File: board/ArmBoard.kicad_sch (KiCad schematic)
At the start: 0 parts

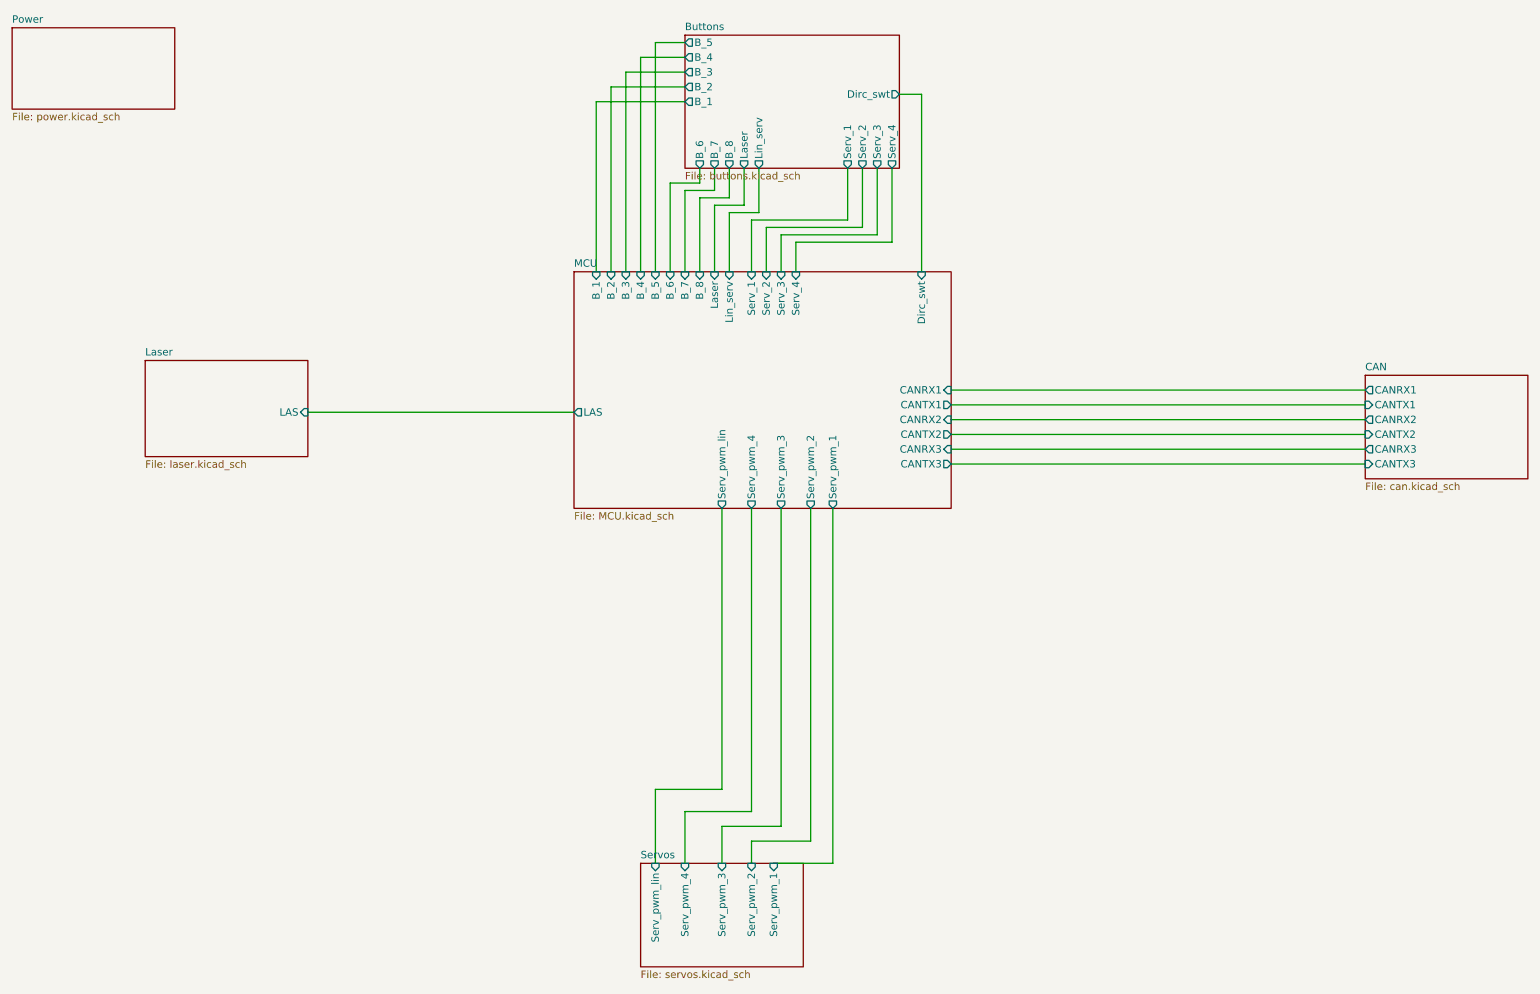
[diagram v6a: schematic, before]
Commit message: Schematic review changes part 2 the electric boogaloo
finished fixing schematic. Made better names for heiracal pins. Made LED ressistors standard values.
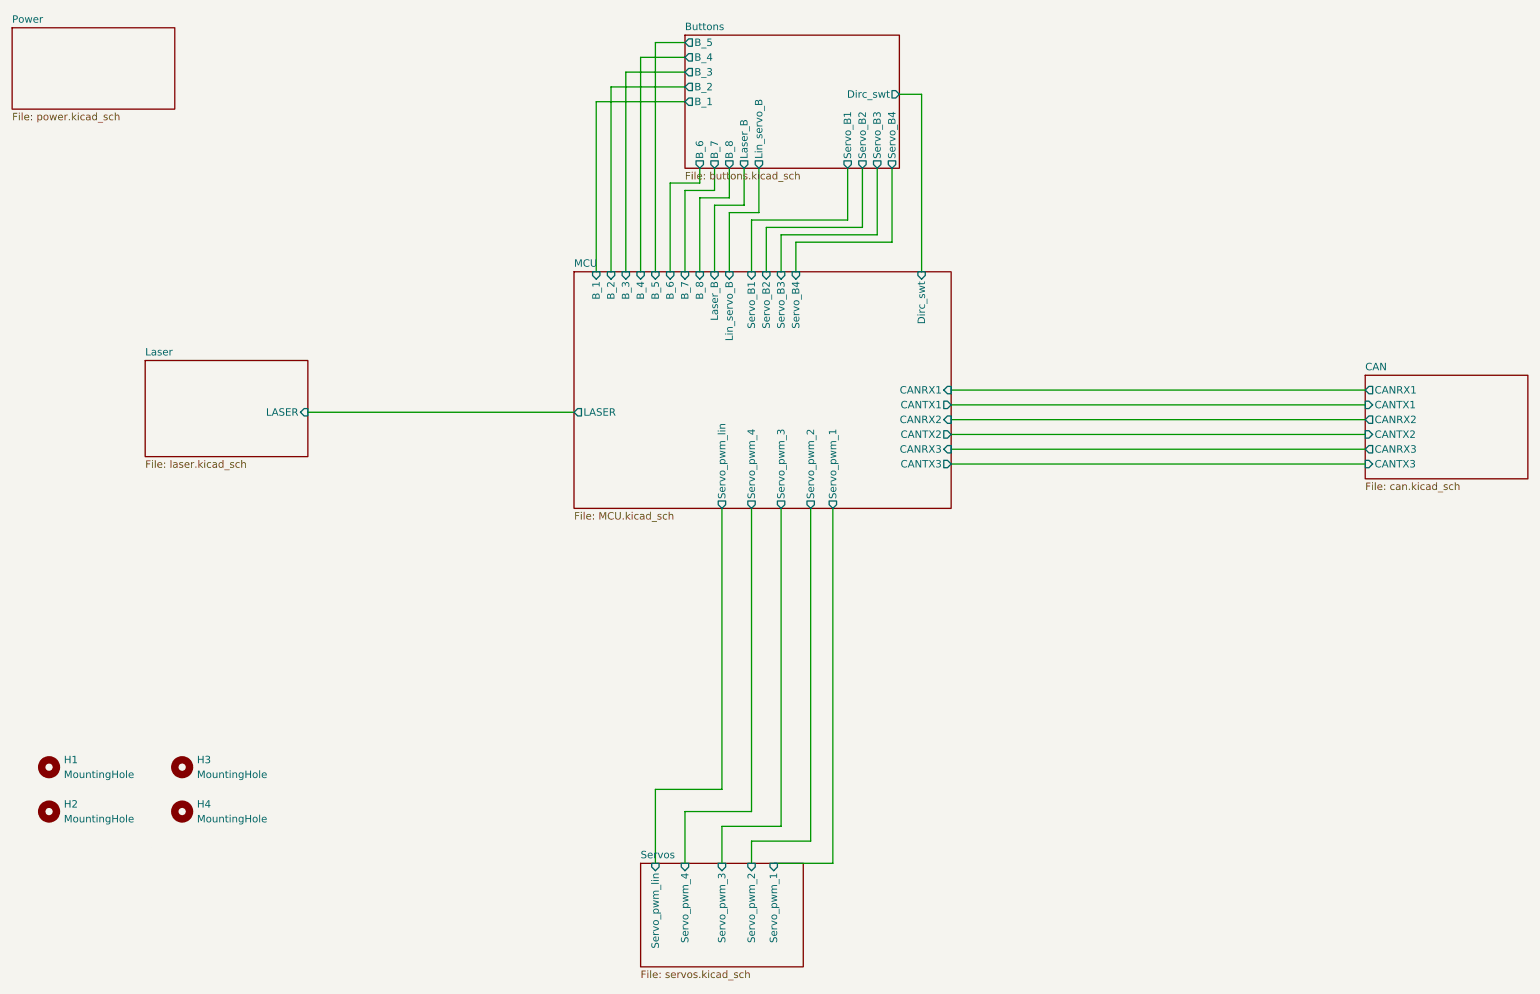
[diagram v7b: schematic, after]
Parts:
- added H1, H2, H3, H4: MountingHole, symbol Mechanical:MountingHole
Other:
- sheet Buttons ports: added Laser_B, Lin_servo_B, Servo_B1, Servo_B2, Servo_B3, Servo_B4; removed Laser, Lin_serv, Serv_1, Serv_2, Serv_3, Serv_4
- sheet Laser ports: added LASER; removed LAS
- sheet MCU ports: added LASER, Laser_B, Lin_servo_B, Servo_B1, Servo_B2, Servo_B3, Servo_B4, Servo_pwm_1, Servo_pwm_2, Servo_pwm_3, Servo_pwm_4, Servo_pwm_lin; removed LAS, Laser, Lin_serv, Serv_1, Serv_2, Serv_3, Serv_4, Serv_pwm_1, Serv_pwm_2, Serv_pwm_3, Serv_pwm_4, Serv_pwm_lin
- sheet Servos ports: added Servo_pwm_1, Servo_pwm_2, Servo_pwm_3, Servo_pwm_4, Servo_pwm_lin; removed Serv_pwm_1, Serv_pwm_2, Serv_pwm_3, Serv_pwm_4, Serv_pwm_lin
- note added: "Penis"

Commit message: Prototype Layout
Made an initial Layout to be edited and changed uwu
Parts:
- H1, H2, H3, H4: footprint (none) -> MRDT_Drill_Holes:4_40_Hole_Corner
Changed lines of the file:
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@@
 			)
 		)
-		(property "Footprint" ""
+		(property "Footprint" "MRDT_Drill_Holes:4_40_Hole_Corner"
 			(at 26.67 149.86 0)
 			(effects
@@
 			)
 		)
-		(property "Footprint" ""
+		(property "Footprint" "MRDT_Drill_Holes:4_40_Hole_Corner"
 			(at 49.53 157.48 0)
 			(effects
@@
 			)
 		)
-		(property "Footprint" ""
+		(property "Footprint" "MRDT_Drill_Holes:4_40_Hole_Corner"
 			(at 26.67 157.48 0)
 			(effects
@@
 			)
 		)
-		(property "Footprint" ""
+		(property "Footprint" "MRDT_Drill_Holes:4_40_Hole_Corner"
 			(at 49.53 149.86 0)
 			(effects
